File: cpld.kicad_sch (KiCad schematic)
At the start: 30 parts, among them IC2 EPM3064ATC44-7N, J1 USB_OTG, J2 INPUTS, J3 OUTPUTS, J4 Conn_ARM_JTAG_SWD_10, SW0 SW_DPDT_x2, SW1 SW_DPDT_x2, SW2 SW_DPDT_x2, SW3 SW_DPDT_x2, U1 AMS1117-3.3, Y1 ECS-TXO-3225-250-TR

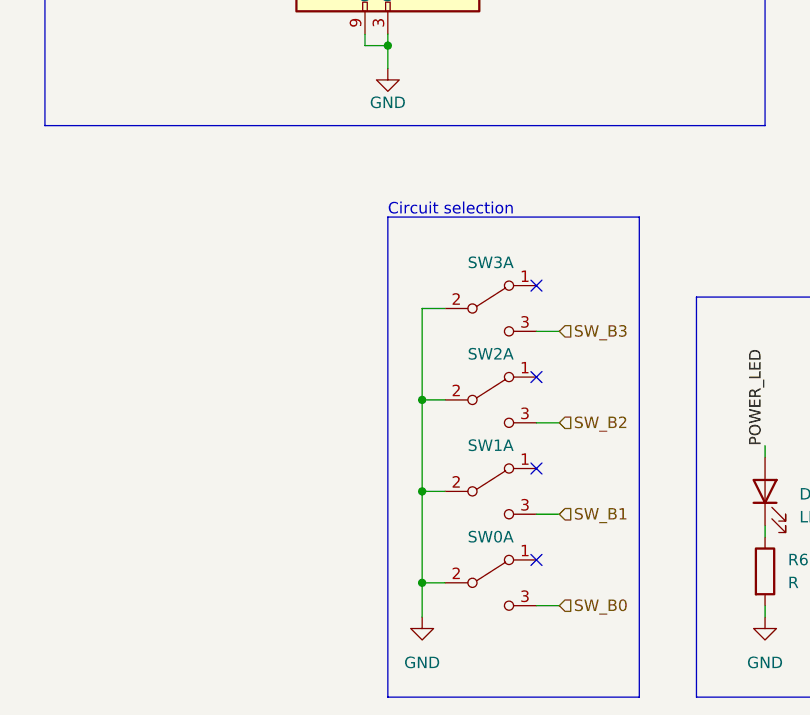
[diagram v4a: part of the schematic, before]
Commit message: added pullups for the switches
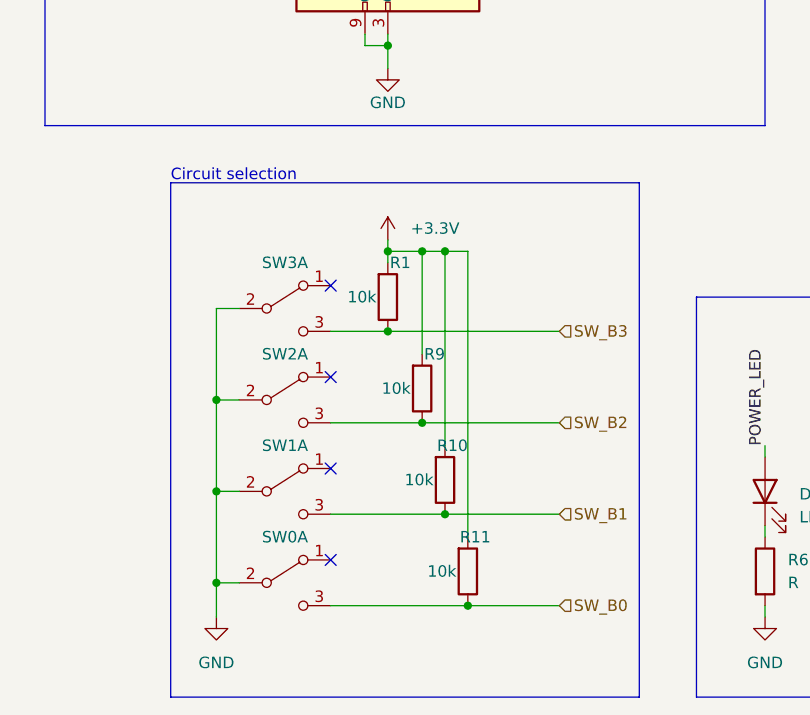
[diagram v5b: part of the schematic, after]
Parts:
- added R1, R10, R11, R9: 10k, Resistor_SMD:R_0603_1608Metric, symbol Device:R
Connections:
- net +3.3V: now also R1.2, R10.2, R11.2, R9.2
- net SW_B0: now also R11.1
- net SW_B1: now also R10.1
- net SW_B2: now also R9.1
- net SW_B3: now also R1.1
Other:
- moved on the sheet: SW0A, SW1A, SW2A, SW3A
